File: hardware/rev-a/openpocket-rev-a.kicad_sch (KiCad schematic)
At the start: 297 parts, among them J1 ER-TFT050A3-2 FFC, J10 RX antenna coax, J11 optional U.FL, J12 push-push microSD, J13 speaker solder pads, J2 USB-C, J3 battery/NTC, J4 speaker connector, J5 master switch, J6 ELRS, J7 left gimbal, J8 right gimbal, J9 controls, Q1 dual protection FET, Q2 Q_BUZZ buzzer MOSFET, U1 ESP32-S3-MINI-1U-N8, U10 display 3V3 buck, U11 analog OSD, U12 OSD 3V3-to-5V, U13 OSD 5V-to-3V3, U14 CVBS TFT controller, U15 AMT boot flash, U16 AMT flash mux, U17 backlight boost, U18 GPIO expander 0x20, U19 GPIO expander 0x21, U2 1S charger/power path, U20 master load switch, U21 I2S speaker amplifier, U22 3V3_SD load switch, U3 1S protector, U4 fuel gauge, U5 3V3 buck-boost, U6 5V boost, U7 5V_VIDEO load switch, U8 5V_DISPLAY load switch, U9 5V_ELRS load switch, Y1 27.000MHz, Y2 27.000MHz

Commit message: feat(hardware): harden Revision-A preproduction design
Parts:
- removed C29: 4.7u 10V, openpocket-easyeda:C0603, symbol openpocket-rev-a:C29_CGA0603X7R475K100JT
- removed C53: 4.7u 10V, openpocket-easyeda:C0603, symbol openpocket-rev-a:C53_CGA0603X7R475K100JT
- removed C6: 470u, openpocket-easyeda:CAP-SMD_BD8.0-L8.3-W8.3-FD, symbol openpocket-rev-a:C6_EEEFK1A471P
- removed R62: 5.1M, openpocket-easyeda:R0402, symbol openpocket-rev-a:R62_RC0402FR-075M1L
- removed R63: 5.1M, openpocket-easyeda:R0402, symbol openpocket-rev-a:R63_RC0402FR-075M1L
- added C29: 4.7u 10V, OpenPocket:0603, symbol openpocket-rev-a:C29_0603B475K100NT
- added C53: 4.7u 10V, OpenPocket:0603, symbol openpocket-rev-a:C53_0603B475K100NT
- added C6: 470u, OpenPocket:SMD-D10, symbol openpocket-rev-a:C6_VZH471M1ATR-1008
- added R62: 5.1M, OpenPocket:0402, symbol openpocket-rev-a:R62_0402WGF5104TCE
- added R63: 5.1M, OpenPocket:0402, symbol openpocket-rev-a:R63_0402WGF5104TCE
- BZ1: DNP (none) -> no; LCSC (none) -> C7421675; MPN (none) -> YS-SBZ7525C05R30; Manufacturer (none) -> Fengming
- C1, C17, C20, C22, C24, C35, C4, C41, C57, C58, C59, C62, C67, C69, C7, C70, C71, C72, C73, C74, C77, C78, C79, C80, C81, C82, C9: DNP (none) -> no; LCSC (none) -> C1525; MPN (none) -> CL05B104KO5NNNC; Manufacturer (none) -> Samsung Electro-Mechanics
- C10, C11, C12: DNP (none) -> no; LCSC (none) -> C1705; MPN (none) -> CL10A475KP8NNNC; Manufacturer (none) -> Samsung Electro-Mechanics
- C15, C16: DNP (none) -> no; LCSC (none) -> C107005; MPN (none) -> CC0402JRNPO9BN330; Manufacturer (none) -> Yageo
- C18, C19, C2, C21, C25, C3, C36, C37, C5, C51, C60, C75: DNP (none) -> no; LCSC (none) -> C15850; MPN (none) -> CL21A106KAYNNNE; Manufacturer (none) -> Samsung Electro-Mechanics
- C23: DNP (none) -> no; LCSC (none) -> C15195; MPN (none) -> CL05B103KB5NNNC; Manufacturer (none) -> Samsung Electro-Mechanics
- C26: DNP (none) -> no; LCSC (none) -> C96123; MPN (none) -> CL31A476MPHNNNE; Manufacturer (none) -> Samsung Electro-Mechanics
- C27, C64, C65, C66: DNP (none) -> no; LCSC (none) -> C14442; MPN (none) -> CL05B102KB5NNNC; Manufacturer (none) -> Samsung Electro-Mechanics
- C28, C31, C34: DNP (none) -> no; LCSC (none) -> C6119932; MPN (none) -> CGA0805X7R106K250MT; Manufacturer (none) -> HRE
- C30, C42: DNP (none) -> no; LCSC (none) -> C272875; MPN (none) -> CC0402KRX7R9BB473; Manufacturer (none) -> Yageo
- C32, C33, C38, C39, C45, C46, C47, C48, C49, C50, C52: DNP (none) -> no; LCSC (none) -> C23692981; MPN (none) -> CGA0805X7R226M100MT; Manufacturer (none) -> HRE
- C40: DNP (none) -> no; LCSC (none) -> C23630; MPN (none) -> CL10A225KO8NNNC; Manufacturer (none) -> Samsung Electro-Mechanics
- C43, C63: DNP (none) -> no; LCSC (none) -> C84705; MPN (none) -> CL05B472KB5NNNC; Manufacturer (none) -> Samsung Electro-Mechanics
- C44: DNP (none) -> no; LCSC (none) -> C84703; MPN (none) -> CL05B222KB5NNNC; Manufacturer (none) -> Samsung Electro-Mechanics
- C54: DNP (none) -> no; LCSC (none) -> C723566; MPN (none) -> CC0402KRX7R8BB224; Manufacturer (none) -> Yageo
- C55, C56: DNP (none) -> no; LCSC (none) -> C91185; MPN (none) -> CC0805KKX7R9BB105; Manufacturer (none) -> Yageo
- C61: DNP (none) -> no; LCSC (none) -> C22435970; MPN (none) -> CGA0402X7R474K160GT; Manufacturer (none) -> HRE
- C68: DNP (none) -> no; LCSC (none) -> C52923; MPN (none) -> CL05A105KA5NQNC; Manufacturer (none) -> Samsung Electro-Mechanics
- C76: DNP (none) -> yes; LCSC (none) -> C401648; MPN (none) -> EEEFK1A221P; Manufacturer (none) -> Panasonic; now left out of the parts list
- C8: DNP (none) -> no; LCSC (none) -> C337699; MPN (none) -> CL05B223KB5NNNC; Manufacturer (none) -> Samsung Electro-Mechanics
- C83: DNP (none) -> yes; LCSC (none) -> C15195; MPN (none) -> CL05B103KB5NNNC; Manufacturer (none) -> Samsung Electro-Mechanics; now left out of the parts list
- D1: DNP (none) -> no; LCSC (none) -> C92506; MPN (none) -> B240A-13-F; Manufacturer (none) -> Diodes Inc
- D2: DNP (none) -> no; LCSC (none) -> C81598; MPN (none) -> 1N4148W; Manufacturer (none) -> LGE
- ESD1, ESD4: DNP (none) -> no; LCSC (none) -> C97502; MPN (none) -> TPD2EUSB30DRTR; Manufacturer (none) -> Texas Instruments
- ESD2, ESD3: DNP (none) -> no; LCSC (none) -> C527516; MPN (none) -> TPD4E001DRLR; Manufacturer (none) -> Texas Instruments
- F1: DNP (none) -> no; LCSC (none) -> C151163; MPN (none) -> 1206L200PR; Manufacturer (none) -> Littelfuse
- FB1: DNP (none) -> no; LCSC (none) -> C85840; MPN (none) -> BLM21PG221SN1D; Manufacturer (none) -> Murata
- FB2, FB3, FB4: DNP (none) -> no; LCSC (none) -> C19330; MPN (none) -> BLM18AG601SN1D; Manufacturer (none) -> Murata
- J1: DNP (none) -> no; LCSC (none) -> C202114; MPN (none) -> FH12-40S-0.5SH(55); Manufacturer (none) -> Hirose
- J10: BOM Comments (none) -> integral coax solder pads; user-wired; DNP (none) -> yes; LCSC (none) -> CONS; MPN (none) -> COAX-SOLDER; Manufacturer (none) -> OpenPocket; now left out of the parts list
- J11: DNP (none) -> yes; LCSC (none) -> C88374; MPN (none) -> U.FL-R-SMT-1(10); Manufacturer (none) -> Hirose; now left out of the parts list
- J12: BOM Comments (none) -> card detect active-low; card ejects toward top edge; DNP (none) -> no; LCSC (none) -> C3021282; MPN (none) -> TF-001A-P3; Manufacturer (none) -> SOFNG
- J13: BOM Comments (none) -> integral differential speaker pads; neither pad is ground; DNP (none) -> yes; LCSC (none) -> CONS; MPN (none) -> SOLDER-PADS-2; Manufacturer (none) -> OpenPocket; now left out of the parts list
- J2: DNP (none) -> no; LCSC (none) -> C3020560; MPN (none) -> USB4105-GF-A; Manufacturer (none) -> GCT
- J3, J7, J8: BOM Comments (none) -> integral solder pads; user-wired, not an assembly item; DNP (none) -> yes; LCSC (none) -> CONS; MPN (none) -> SOLDER-PADS-4; Manufacturer (none) -> OpenPocket; now left out of the parts list
- J4: DNP (none) -> no; LCSC (none) -> C295747; MPN (none) -> S2B-PH-SM4-TB(LF)(SN); Manufacturer (none) -> JST
- J5: BOM Comments (none) -> integral solder pads; user-wired, not an assembly item; DNP (none) -> yes; LCSC (none) -> CONS; MPN (none) -> SOLDER-PADS-2; Manufacturer (none) -> OpenPocket; now left out of the parts list
- J6: BOM Comments (none) -> integral solder pads; user-wired, not an assembly item; DNP (none) -> yes; LCSC (none) -> CONS; MPN (none) -> SOLDER-PADS-6; Manufacturer (none) -> OpenPocket; now left out of the parts list
- J9: BOM Comments (none) -> integral solder pads; user-wired, not an assembly item; DNP (none) -> yes; LCSC (none) -> CONS; MPN (none) -> SOLDER-PADS-22; Manufacturer (none) -> OpenPocket; now left out of the parts list
- JP1: BOM Comments (none) -> factory hand-bridge pads 1-2 and 4-5; bypass cuts both and 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; DNP (none) -> yes; LCSC (none) -> N/A; MPN (none) -> SJ-DPDT; Manufacturer (none) -> OpenPocket; now left out of the parts list
- L1: DNP (none) -> no; LCSC (none) -> C36409; MPN (none) -> SWPA4030S2R2MT; Manufacturer (none) -> Sunlord
- L2: DNP (none) -> no; LCSC (none) -> C142484; MPN (none) -> SWPA4020S1R0MT; Manufacturer (none) -> Sunlord
- L3: DNP (none) -> no; LCSC (none) -> C19191693; MPN (none) -> XAL6030-182MEC; Manufacturer (none) -> Coilcraft
- L4: DNP (none) -> no; LCSC (none) -> C82398; MPN (none) -> SWPA4020S100MT; Manufacturer (none) -> Sunlord
- L5: DNP (none) -> no; LCSC (none) -> C43389; MPN (none) -> SWPA3015S2R2MT; Manufacturer (none) -> Sunlord
- MOD1: BOM Comments (none) -> pre-order or consigned; DNP (none) -> no; LCSC (none) -> C2908157; MPN (none) -> RX5808 SPI-modified; Manufacturer (none) -> WREKD
- Q1: DNP (none) -> no; LCSC (none) -> C908265; MPN (none) -> FS8205A; Manufacturer (none) -> FUXINSEMI
- Q2: DNP (none) -> no; LCSC (none) -> C20917; MPN (none) -> AO3400A; Manufacturer (none) -> Alpha & Omega
- R1, R2: DNP (none) -> no; LCSC (none) -> C105872; MPN (none) -> RC0402FR-075K1L; Manufacturer (none) -> Yageo
- R10: DNP (none) -> no; LCSC (none) -> C245924; MPN (none) -> RC0603FR-0718RL; Manufacturer (none) -> Yageo
- R100, R58, R59, R60, R61, R99: DNP (none) -> no; LCSC (none) -> C138002; MPN (none) -> RC0402FR-0733RL; Manufacturer (none) -> Yageo
- R101: DNP (none) -> no; LCSC (none) -> C106231; MPN (none) -> RC0402FR-070RL; Manufacturer (none) -> Yageo
- R102: DNP (none) -> yes; LCSC (none) -> C106232; MPN (none) -> RC0402FR-07100RL; Manufacturer (none) -> Yageo; now left out of the parts list
- R103: DNP (none) -> no; LCSC (none) -> C112309; MPN (none) -> RC0603FR-0775RL; Manufacturer (none) -> Yageo
- R104, R3, R30, R31, R32, R33, R34, R35, R4, R43, R44, R45, R48, R49, R50, R70, R71, R72, R73, R74, R75, R76, R77, R78, R79, R80, R81, R82, R83, R84, R85, R86, R87, R88, R89, R90, R91, R92, R93, R94: DNP (none) -> no; LCSC (none) -> C60490; MPN (none) -> RC0402FR-0710KL; Manufacturer (none) -> Yageo
- R11: DNP (none) -> no; LCSC (none) -> C126360; MPN (none) -> RC0603FR-0756RL; Manufacturer (none) -> Yageo
- R12, R13, R16, R21, R36, R40, R41, R5, R66, R67, R68, R69, R7, R8: DNP (none) -> no; LCSC (none) -> C60491; MPN (none) -> RC0402FR-07100KL; Manufacturer (none) -> Yageo
- R14, R15: DNP (none) -> no; LCSC (none) -> C114762; MPN (none) -> RC0402FR-072K2L; Manufacturer (none) -> Yageo
- R18, R22, R54: DNP (none) -> no; LCSC (none) -> C138033; MPN (none) -> RC0402FR-071ML; Manufacturer (none) -> Yageo
- R20, R23: DNP (none) -> no; LCSC (none) -> C185427; MPN (none) -> RC0402FR-07316KL; Manufacturer (none) -> Yageo
- R24: DNP (none) -> no; LCSC (none) -> C93947; MPN (none) -> RC0402FR-07150KL; Manufacturer (none) -> Yageo
- R25, R53, R64, R65, R95, R96, R97, R98: DNP (none) -> no; LCSC (none) -> C106235; MPN (none) -> RC0402FR-071KL; Manufacturer (none) -> Yageo
- R26: DNP (none) -> no; LCSC (none) -> C114760; MPN (none) -> RC0402FR-0712KL; Manufacturer (none) -> Yageo
- R27: DNP (none) -> no; LCSC (none) -> C138044; MPN (none) -> RC0402FR-0718KL; Manufacturer (none) -> Yageo
- R28, R29, R37, R38, R39: DNP (none) -> no; LCSC (none) -> C138021; MPN (none) -> RC0402FR-0727RL; Manufacturer (none) -> Yageo
- R42: DNP (none) -> no; LCSC (none) -> C137936; MPN (none) -> RC0402FR-07750RL; Manufacturer (none) -> Yageo
- R46: DNP (none) -> no; LCSC (none) -> C477746; MPN (none) -> RC0402FR-075K23L; Manufacturer (none) -> Yageo
- R47: DNP (none) -> no; LCSC (none) -> C138009; MPN (none) -> RC0402FR-0730K1L; Manufacturer (none) -> Yageo
- R51: DNP (none) -> no; LCSC (none) -> C138006; MPN (none) -> RC0402FR-07330KL; Manufacturer (none) -> Yageo
- R52: DNP (none) -> no; LCSC (none) -> C274351; MPN (none) -> RC0402FR-0718K2L; Manufacturer (none) -> Yageo
- R55: DNP (none) -> no; LCSC (none) -> C138066; MPN (none) -> RC0402FR-0710RL; Manufacturer (none) -> Yageo
- R56: DNP (none) -> no; LCSC (none) -> C25104; MPN (none) -> 0402WGF3300TCE; Manufacturer (none) -> Uniroyal Electronics
- R57: DNP (none) -> no; LCSC (none) -> C25879; MPN (none) -> 0402WGF2201TCE; Manufacturer (none) -> Uniroyal Electronics
- R6: DNP (none) -> no; LCSC (none) -> C106232; MPN (none) -> RC0402FR-07100RL; Manufacturer (none) -> Yageo
- R9: DNP (none) -> no; LCSC (none) -> C137704; MPN (none) -> RC0603FR-074R99L; Manufacturer (none) -> Yageo
- TP1, TP10, TP11, TP12, TP13, TP14, TP15, TP16, TP17, TP18, TP19, TP2, TP20, TP21, TP22, TP23, TP24, TP25, TP26, TP27, TP28, TP29, TP3, TP30, TP31, TP32, TP33, TP34, TP35, TP36, TP37, TP38, TP39, TP4, TP40, TP41, TP42, TP43, TP44, TP45, TP46, TP47, TP48, TP49, TP5, TP50, TP51, TP52, TP53, TP54, TP55, TP6, TP7, TP8, TP9: BOM Comments (none) -> bare ENIG copper test feature; not an assembled component; DNP (none) -> yes; LCSC (none) -> N/A; MPN (none) -> PCB-TEST-PAD-1.0MM; Manufacturer (none) -> OpenPocket; now left out of the parts list
- TVS1: DNP (none) -> no; LCSC (none) -> C82044; MPN (none) -> ESD5Z5.0T1G; Manufacturer (none) -> onsemi
- U1: DNP (none) -> no; LCSC (none) -> C2980299; MPN (none) -> ESP32-S3-MINI-1U-N8; Manufacturer (none) -> Espressif
- U10: DNP (none) -> no; LCSC (none) -> C40256; MPN (none) -> TPS62162DSGR; Manufacturer (none) -> Texas Instruments
- U11: DNP (none) -> no; LCSC (none) -> C82351; MPN (none) -> AT7456E; Manufacturer (none) -> Zhongkewei
- U12: DNP (none) -> no; LCSC (none) -> C36365; MPN (none) -> SN74AHCT125PWR; Manufacturer (none) -> Texas Instruments
- U13: DNP (none) -> no; LCSC (none) -> C9382; MPN (none) -> SN74LVC1T45DCKR; Manufacturer (none) -> Texas Instruments
- U14: DNP (none) -> no; LCSC (none) -> C9900018923; MPN (none) -> AMT630A; Manufacturer (none) -> Actions Microelectronics
- U15: DNP (none) -> no; LCSC (none) -> C2641187; MPN (none) -> W25X05CLSNIG; Manufacturer (none) -> Winbond
- U16: DNP (none) -> no; LCSC (none) -> C397142; MPN (none) -> SN74CB3Q3257PWR; Manufacturer (none) -> Texas Instruments
- U17: DNP (none) -> no; LCSC (none) -> C122568; MPN (none) -> TPS61165DRVR; Manufacturer (none) -> Texas Instruments
- U18, U19: DNP (none) -> no; LCSC (none) -> C130204; MPN (none) -> TCA9535PWR; Manufacturer (none) -> Texas Instruments
- U2: DNP (none) -> no; LCSC (none) -> C80200; MPN (none) -> BQ25895RTWR; Manufacturer (none) -> Texas Instruments
- U20: DNP (none) -> no; LCSC (none) -> C3229354; MPN (none) -> TPS22992SRXNR; Manufacturer (none) -> Texas Instruments
- U21: DNP (none) -> no; LCSC (none) -> C910588; MPN (none) -> NS4168; Manufacturer (none) -> Nsiway
- U22, U7, U8, U9: DNP (none) -> no; LCSC (none) -> C131941; MPN (none) -> TPS22918DBVR; Manufacturer (none) -> Texas Instruments
- U3: DNP (none) -> no; LCSC (none) -> C183096; MPN (none) -> BQ29700DSER; Manufacturer (none) -> Texas Instruments
- U4: DNP (none) -> no; LCSC (none) -> C2682616; MPN (none) -> MAX17048G+T10; Manufacturer (none) -> Analog Devices
- U5: DNP (none) -> no; LCSC (none) -> C109322; MPN (none) -> TPS63070RNMR; Manufacturer (none) -> Texas Instruments
- U6: DNP (none) -> no; LCSC (none) -> C87357; MPN (none) -> TPS61088RHLR; Manufacturer (none) -> Texas Instruments
- Y1, Y2: DNP (none) -> no; LCSC (none) -> C1985251; MPN (none) -> ABM8-27.000MHZ-B2-T; Manufacturer (none) -> Abracon
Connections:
- net 5V_DISPLAY: now also C53.1
- net 5V_VIDEO_FILT: now also C6.1
- net BAT_CELL_NEG: now also R62.2
- net GND: now also C29.2, C53.2, C6.2, R63.2
- net PROT_COUT: now also R63.1
- net PROT_DOUT: now also R62.1
- net REGN: now also C29.1

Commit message: hardware: establish reviewed eight-layer Rev A basis
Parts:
- removed J10: RX antenna coax, OpenPocket:COAX-SOLDER, symbol openpocket-rev-a:J10_COAX-SOLDER
- J11: value optional U.FL -> 5.8 GHz antenna U.FL; BOM Comments (none) -> populate; accepts U.FL/MHF1 cable plug vertically from top; DNP yes -> no; now in the parts list

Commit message: hardware: finalize bottom-side U.FL sourcing
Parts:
- J11: LCSC C88374 -> C88373
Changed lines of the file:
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@@
 			)
 		)
-		(property "LCSC" "C88374"
+		(property "LCSC" "C88373"
 			(at 104.14 304.7999 0)
 			(effects

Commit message: feat(hardware): checkpoint connector placement and routing assets
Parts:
- removed J7: left gimbal, OpenPocket:EDGE-PADS-4, symbol openpocket-rev-a:J7_SOLDER-PADS-4
- removed J8: right gimbal, OpenPocket:EDGE-PADS-4, symbol openpocket-rev-a:J8_SOLDER-PADS-4
- added J14: SSD1306 128x64 OLED pads, OpenPocket:DEV-PADS-4, symbol openpocket-rev-a:J14_DEV-PADS-4
- added J15: expander developer pads, OpenPocket:DEV-PADS-6, symbol openpocket-rev-a:J15_DEV-PADS-6
- added J16: controls ground pads, OpenPocket:EDGE-PADS-2, symbol openpocket-rev-a:J16_SOLDER-PADS-2
- added J7: left gimbal, OpenPocket:EDGE-PADS-6, symbol openpocket-rev-a:J7_SOLDER-PADS-6
- added J8: right gimbal, OpenPocket:EDGE-PADS-6, symbol openpocket-rev-a:J8_SOLDER-PADS-6
- J11: footprint openpocket-easyeda:RF-SMD_FRF05002-JSS103M -> OpenPocket:U.FL; BOM Comments populate; accepts U.FL/MHF1 cable plug vertically from top -> populate on bottom; accepts U.FL/MHF1 plug vertically; secu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
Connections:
- net 3V3_LOGIC: now also J14.2 (VCC), J15.5 (3V3), J7.2 (LX_VCC), J7.5 (LY_VCC), J8.2 (RX_VCC), J8.5 (RY_VCC)
- net GIMBAL_LX_RAW: now also J7.1 (LX)
- net GIMBAL_LY_RAW: now also J7.4 (LY)
- net GIMBAL_RX_RAW: now also J8.1 (RX)
- net GIMBAL_RY_RAW: now also J8.4 (RY)
- net GND: now also J14.1 (GND), J15.6 (GND), J16.1 (GND1), J16.2 (GND2), J7.3 (LX_GND), J7.6 (LY_GND), J8.3 (RX_GND), J8.6 (RY_GND)
- net I2C_SCL: now also J14.4 (SCL)
- net I2C_SDA: now also J14.3 (SDA)
- net DEV_IO0: now reaches U19.17 (P14)
- net DEV_IO0: now also J15.1 (IO0)
- net DEV_IO1: now reaches U19.18 (P15)
- net DEV_IO1: now also J15.2 (IO1)
- net DEV_IO2: now reaches U19.19 (P16)
- net DEV_IO2: now also J15.3 (IO2)
- net DEV_IO3: now reaches U19.20 (P17)
- net DEV_IO3: now also J15.4 (IO3)
- no-connect marks 25 -> 21

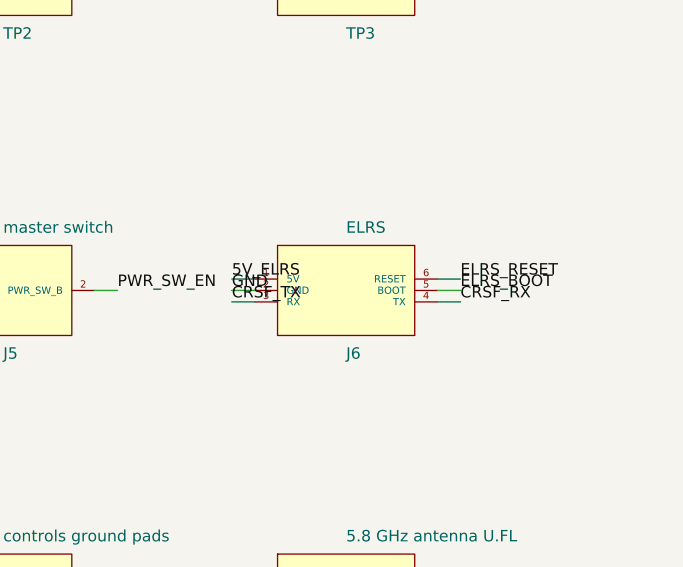
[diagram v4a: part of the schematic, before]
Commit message: feat(rev-a): add deterministic placement optimizer
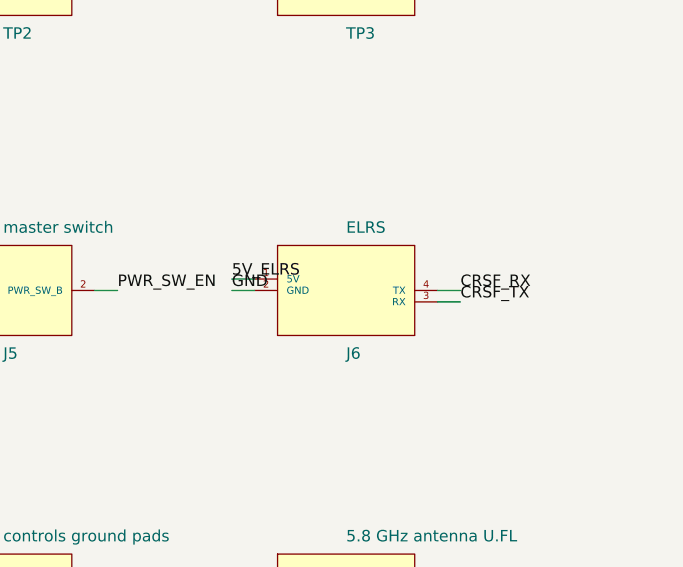
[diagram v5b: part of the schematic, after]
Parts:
- removed J6: ELRS, OpenPocket:EDGE-PADS-6, symbol openpocket-rev-a:J6_SOLDER-PADS-6
- added J6: ELRS, OpenPocket:EDGE-PADS-4, symbol openpocket-rev-a:J6_SOLDER-PADS-4
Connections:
- net 5V_ELRS: now also J6.1 (5V)
- net CRSF_RX: now also J6.4 (TX)
- net CRSF_TX: now also J6.3 (RX)
- net GND: now also J6.2 (GND)

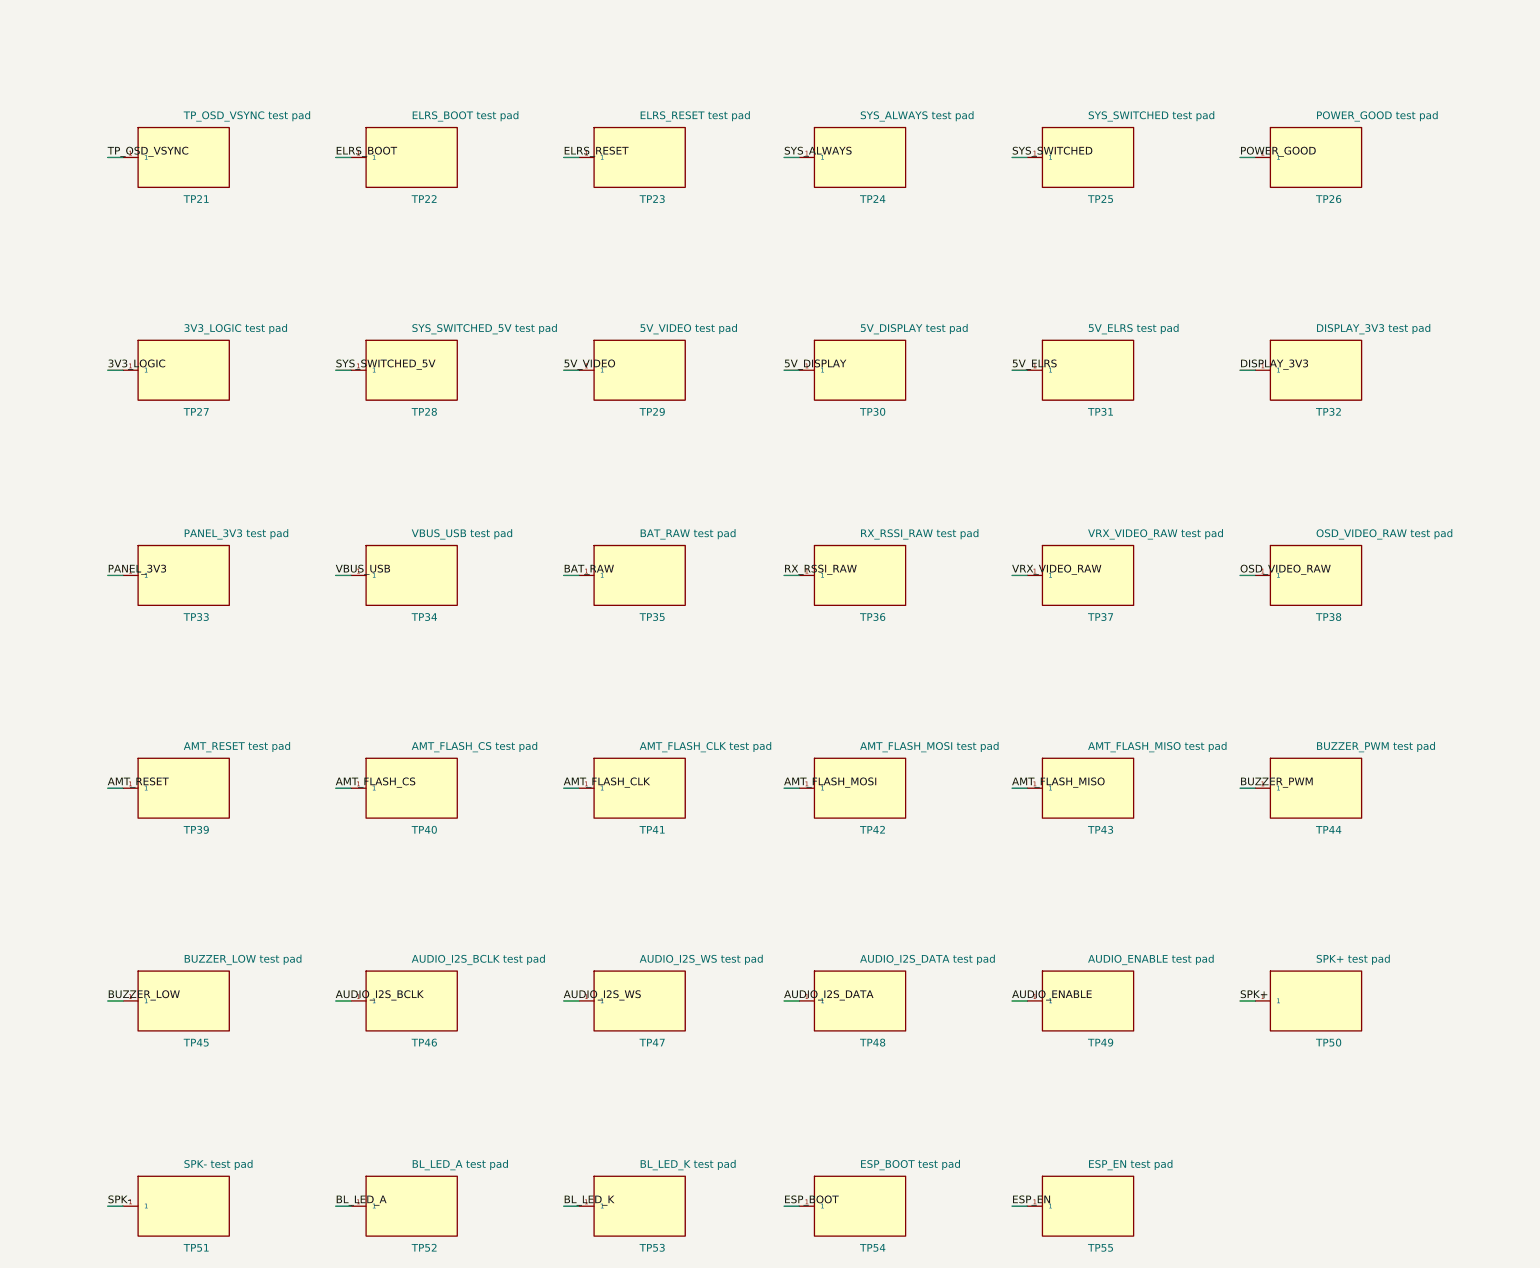
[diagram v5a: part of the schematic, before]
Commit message: fix(rev-a): remove dangling ELRS debug labels and refresh renders
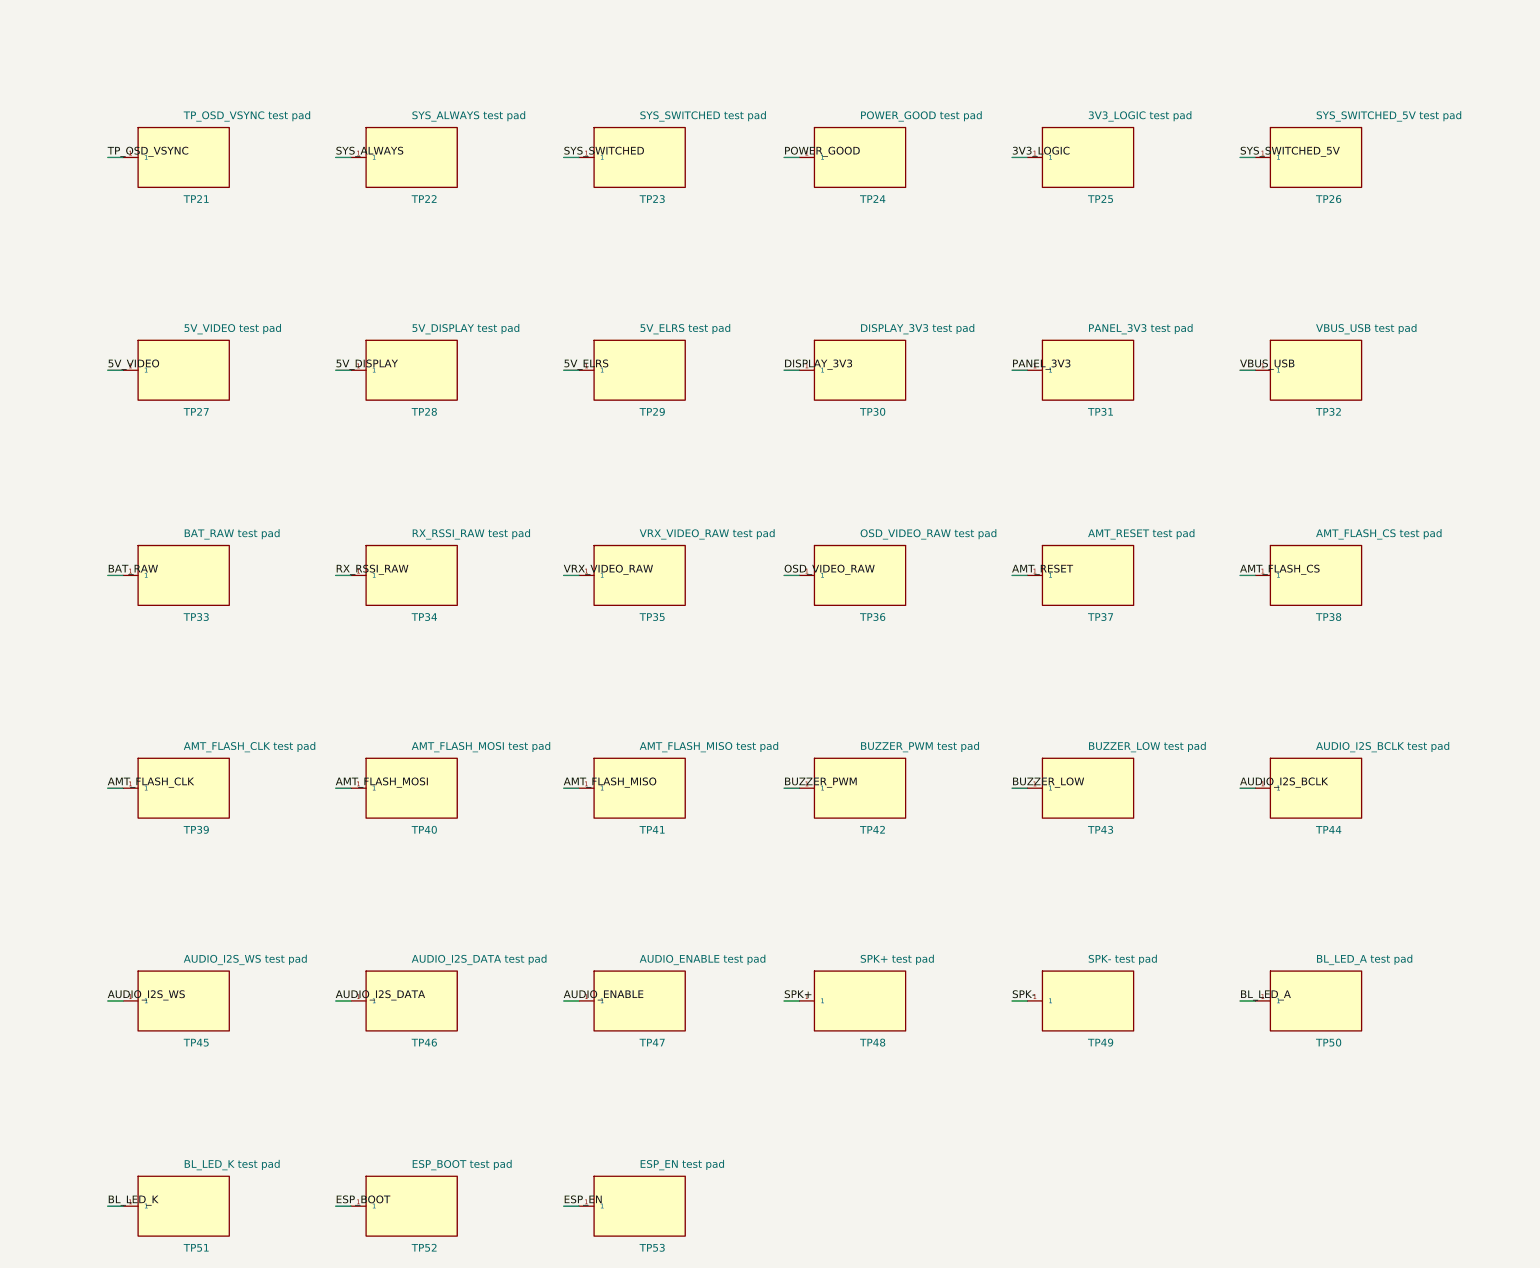
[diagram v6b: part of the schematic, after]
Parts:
- removed TP54: ESP_BOOT test pad, OpenPocket:TEST-PAD-1.0MM, symbol openpocket-rev-a:TP54_PCB-TEST-PAD-1.0MM
- removed TP55: ESP_EN test pad, OpenPocket:TEST-PAD-1.0MM, symbol openpocket-rev-a:TP55_PCB-TEST-PAD-1.0MM
- TP22: value ELRS_BOOT test pad -> SYS_ALWAYS test pad
- TP23: value ELRS_RESET test pad -> SYS_SWITCHED test pad
- TP24: value SYS_ALWAYS test pad -> POWER_GOOD test pad
- TP25: value SYS_SWITCHED test pad -> 3V3_LOGIC test pad
- TP26: value POWER_GOOD test pad -> SYS_SWITCHED_5V test pad
- TP27: value 3V3_LOGIC test pad -> 5V_VIDEO test pad
- TP28: value SYS_SWITCHED_5V test pad -> 5V_DISPLAY test pad
- TP29: value 5V_VIDEO test pad -> 5V_ELRS test pad
- TP30: value 5V_DISPLAY test pad -> DISPLAY_3V3 test pad
- TP31: value 5V_ELRS test pad -> PANEL_3V3 test pad
- TP32: value DISPLAY_3V3 test pad -> VBUS_USB test pad
- TP33: value PANEL_3V3 test pad -> BAT_RAW test pad
- TP34: value VBUS_USB test pad -> RX_RSSI_RAW test pad
- TP35: value BAT_RAW test pad -> VRX_VIDEO_RAW test pad
- TP36: value RX_RSSI_RAW test pad -> OSD_VIDEO_RAW test pad
- TP37: value VRX_VIDEO_RAW test pad -> AMT_RESET test pad
- TP38: value OSD_VIDEO_RAW test pad -> AMT_FLASH_CS test pad
- TP39: value AMT_RESET test pad -> AMT_FLASH_CLK test pad
- TP40: value AMT_FLASH_CS test pad -> AMT_FLASH_MOSI test pad
- TP41: value AMT_FLASH_CLK test pad -> AMT_FLASH_MISO test pad
- TP42: value AMT_FLASH_MOSI test pad -> BUZZER_PWM test pad
- TP43: value AMT_FLASH_MISO test pad -> BUZZER_LOW test pad
- TP44: value BUZZER_PWM test pad -> AUDIO_I2S_BCLK test pad
- TP45: value BUZZER_LOW test pad -> AUDIO_I2S_WS test pad
- TP46: value AUDIO_I2S_BCLK test pad -> AUDIO_I2S_DATA test pad
- TP47: value AUDIO_I2S_WS test pad -> AUDIO_ENABLE test pad
- TP48: value AUDIO_I2S_DATA test pad -> SPK+ test pad
- TP49: value AUDIO_ENABLE test pad -> SPK- test pad
- TP50: value SPK+ test pad -> BL_LED_A test pad
- TP51: value SPK- test pad -> BL_LED_K test pad
- TP52: value BL_LED_A test pad -> ESP_BOOT test pad
- TP53: value BL_LED_K test pad -> ESP_EN test pad
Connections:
- net ELRS_BOOT is gone; now on net SYS_ALWAYS: TP22.1
- net ELRS_RESET is gone; now on net SYS_SWITCHED: TP23.1
- net 3V3_LOGIC: now also TP25.1; no longer TP27.1
- net 5V_DISPLAY: now also TP28.1; no longer TP30.1
- net 5V_ELRS: now also TP29.1; no longer TP31.1
- net 5V_VIDEO: now also TP27.1; no longer TP29.1
- net AMT_FLASH_CLK: now also TP39.1; no longer TP41.1
- net AMT_FLASH_CS: now also TP38.1; no longer TP40.1
- net AMT_FLASH_MISO: now also TP41.1; no longer TP43.1
- net AMT_FLASH_MOSI: now also TP40.1; no longer TP42.1
- net AMT_RESET: now also TP37.1; no longer TP39.1
- net AUDIO_ENABLE: now also TP47.1; no longer TP49.1
- net AUDIO_I2S_BCLK: now also TP44.1; no longer TP46.1
- net AUDIO_I2S_DATA: now also TP46.1; no longer TP48.1
- net AUDIO_I2S_WS: now also TP45.1; no longer TP47.1
- net BAT_RAW: now also TP33.1; no longer TP35.1
- net BL_LED_A: now also TP50.1; no longer TP52.1
- net BL_LED_K: now also TP51.1; no longer TP53.1
- net BUZZER_LOW: now also TP43.1; no longer TP45.1
- net BUZZER_PWM: now also TP42.1; no longer TP44.1
- net DISPLAY_3V3: now also TP30.1; no longer TP32.1
- net ESP_BOOT: now also TP52.1
- net ESP_EN: now also TP53.1
- net OSD_VIDEO_RAW: now also TP36.1; no longer TP38.1
- net PANEL_3V3: now also TP31.1; no longer TP33.1
- net POWER_GOOD: now also TP24.1; no longer TP26.1
- net RX_RSSI_RAW: now also TP34.1; no longer TP36.1
- net SPK+: now also TP48.1; no longer TP50.1
- net SPK-: now also TP49.1; no longer TP51.1
- net SYS_ALWAYS: no longer TP24.1
- net SYS_SWITCHED: no longer TP25.1
- net SYS_SWITCHED_5V: now also TP26.1; no longer TP28.1
- net VBUS_USB: now also TP32.1; no longer TP34.1
- net VRX_VIDEO_RAW: now also TP35.1; no longer TP37.1
